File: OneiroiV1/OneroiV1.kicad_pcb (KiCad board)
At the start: 4 copper layers, 50 x 75 mm, 164 parts, among them J1 Conn_02x04_Odd_Even, J10 MSD-10-C, J12 Conn_01x06, J13 TB002-500-02BE, J14 TB002-500-02BE, J15 TB002-500-02BE, J16 TB002-500-02BE, J17 TB002-500-02BE, J18 TB002-500-02BE, J19 TB002-500-02BE, J20 TB002-500-02BE, J21 TB002-500-02BE, J22 TB002-500-02BE, J3 USB4110GFA, J4 Conn_01x02, J5 3-1478978-1, J6 Conn_02x04_Odd_Even, J7 Conn_02x02_Odd_Even, J9 MSD-10-C, Q1 SI4909DY-T1-GE3, Q2 MBT3904DW1T1G, U1 LSM6DSV80XTR, U13 TPS2121RUXT, U14 TPS2121RUXT, U15 H3LIS331DLTR, U16 ESDS302DBVR, U17 ESDS302DBVR, U18 MS561101BA03-50, U19 MS561101BA03-50, U2 MAX-M10S-00B, U20 BMI323, U21 BMI270, U22 TPS63070RNMR, U23 TPS63070RNMR, U24 ESDS302DBVR, U25 ESDS302DBVR, U3 ESP32-S3-WROOM-1U-N4, U4 DMP3085LSD-13, U5 CVJ10F30_LF, U7 MMDT5551-7-F, U8 LDL1117S33R, U9 LM66200DRLR

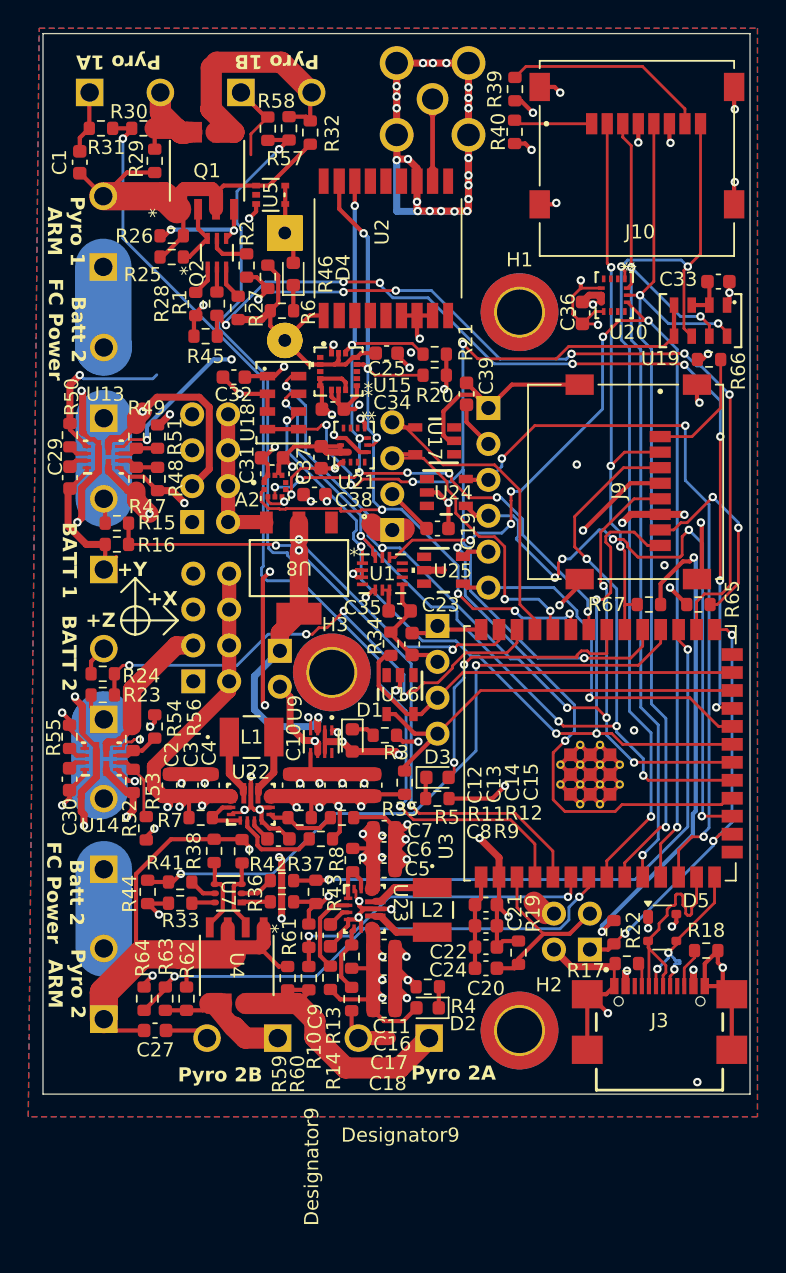
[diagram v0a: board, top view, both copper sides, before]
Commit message: Oneiroi Changes
All 3D models and footprints updated to common library, silkscreening must be re-done.
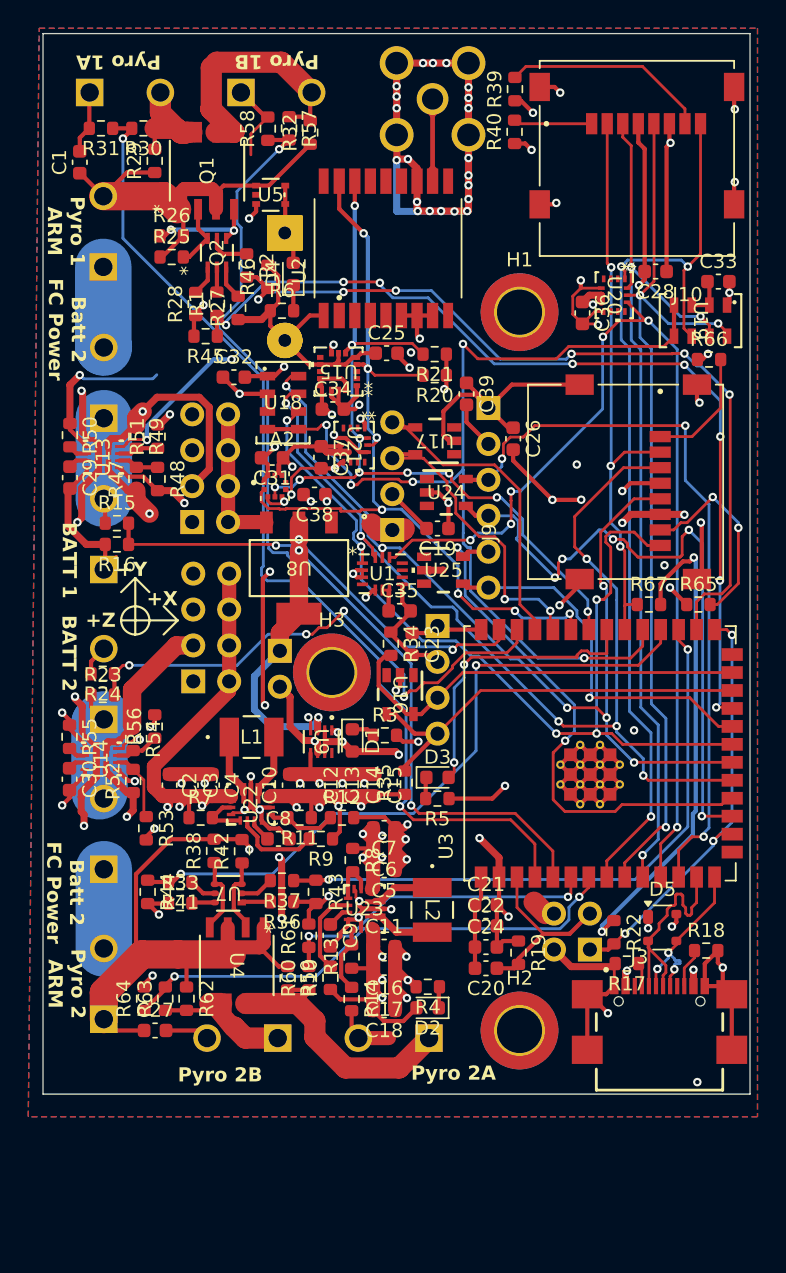
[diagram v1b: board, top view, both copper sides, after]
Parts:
- added C26: 100nF, Capacitor_SMD:C_0603_1608Metric, F.Cu at (143.2, 68.7)
- added C28: 100nF, Capacitor_SMD:C_0603_1608Metric, F.Cu at (153.3, 56.8)
- A2: footprint Baro 1:XDCR_LPS22DFTR -> UNSW Rocketry Library:XDCR_LPS22DFTR
- G***: footprint Logos:RocketryLogoSmall -> UNSW Rocketry Library:RocketryLogoSmall
- G***: footprint Logos:Storm -> UNSW Rocketry Library:Storm
- G***: footprint Logos:Butterfly -> UNSW Rocketry Library:Butterfly
- J10, J9: footprint locking microSD:CUI_MSD-10-C -> UNSW Rocketry Library:CUI_MSD-10-C
- J13, J14, J15, J16, J17, J18, J19, J20, J21, J22: footprint screw terminal:CUI_TB002-500-02BE -> UNSW Rocketry Library:CUI_TB002-500-02BE
- J3: footprint USB:GCT_USB4110GFA -> UNSW Rocketry Library:GCT_USB4110GFA
- J5: footprint SMA right angle:TE_3-1478978-1 -> UNSW Rocketry Library:TE_3-1478978-1
- L1, L2: footprint inductor:1277AS-H-1R0M=P2_MUR-M -> UNSW Rocketry Library:1277AS-H-1R0M=P2_MUR-M
- LS1: footprint low volt buzzer:SPKR_CMI-1295-03TH -> UNSW Rocketry Library:SPKR_CMI-1295-03TH
- LS2: footprint better buzzer:CUI_CPI-1375-80T -> UNSW Rocketry Library:CUI_CPI-1375-80T
- Q1: footprint pyro 1:SOIC_09DY-T1-GE3_VIS -> UNSW Rocketry Library:SOIC_09DY-T1-GE3_VIS
- Q2: footprint npn 1:SOT-363&slash_SC-88&slash_SC70-6&slash_CASE419B_OSI -> UNSW Rocketry Library:SOT-363&slash_SC-88&slash_SC70-6&slash_CASE419B_OSI
- U1: footprint Acc 1:QFN_LSM6DSV80XTR_STM -> UNSW Rocketry Library:QFN_LSM6DSV80XTR_STM
- U13, U14: footprint TPS2121:RUX0012A -> UNSW Rocketry Library:RUX0012A
- U15: footprint high-g acc:QFN_31DLTR_STM -> UNSW Rocketry Library:QFN_31DLTR_STM
- U16, U17, U24, U25: footprint esd:DBV0005A_N -> UNSW Rocketry Library:DBV0005A_N
- U18, U19: footprint ms5611:SON8_MS5611_TEC -> UNSW Rocketry Library:SON8_MS5611_TEC
- U2: footprint GPS:XCVR_MAX-M10S-00B -> UNSW Rocketry Library:XCVR_MAX-M10S-00B
- U20: footprint BMI323:BMI323_BOS -> UNSW Rocketry Library:BMI323_BOS
- U21: footprint BMI270:BMI270_BOS -> UNSW Rocketry Library:BMI270_BOS
- U22, U23: footprint TPS63070:RNM0015A -> UNSW Rocketry Library:RNM0015A
- U3: footprint ESP32-S3:XCVR_ESP32-S3-WROOM-1U-N4 -> UNSW Rocketry Library:XCVR_ESP32-S3-WROOM-1U-N4
- U4: footprint pyro 2:IC_DMP3028LSD-13_DIO -> UNSW Rocketry Library:IC_DMP3028LSD-13_DIO
- U5: footprint Diode Chip:UFV_TOS -> UNSW Rocketry Library:UFV_TOS
- U7: footprint npn 2:SOT-363_DIO -> UNSW Rocketry Library:SOT-363_DIO
- U8: footprint LDO:SOT223_STM -> UNSW Rocketry Library:SOT223_STM
- U9: footprint Ideal Diode:SOT-5X3_DRL_TEX -> UNSW Rocketry Library:SOT-5X3_DRL_TEX
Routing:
- net GND: track 391.1 -> 402.6 mm
- net +3.3VA: track 306.4 -> 312.4 mm, vias 15 -> 17
- net +3.3VB: track 127.8 -> 131.7 mm
- net GPIO8: track 51.5 -> 52.0 mm

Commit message: Silkscreen Oneiroi
Adds silkscreen to Oneroi
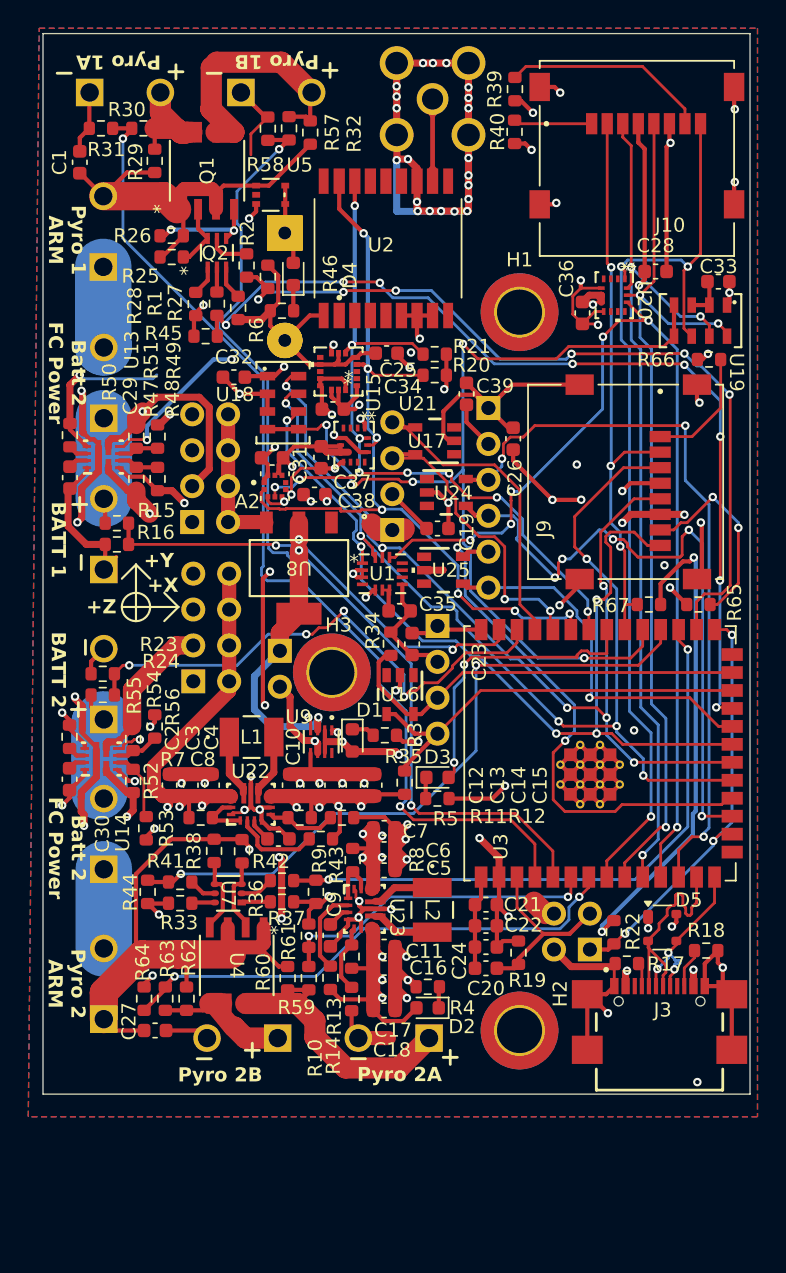
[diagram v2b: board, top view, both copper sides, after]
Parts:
- removed the G*** at (154.3, 85.2)
- removed the G*** at (144.5, 95.8)
- added G***: LOGO, UNSW Rocketry Library:Butterfly_Invert, B.Cu at (149.2, 90.2)
- added G***: LOGO, UNSW Rocketry Library:Storm_Large, B.Cu at (151.2, 90.2)
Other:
- board text added: "Oneiroi V1"
- board text removed: "Oneroi V1"
